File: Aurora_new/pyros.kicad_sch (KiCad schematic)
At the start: 19 parts, among them J10 Screw_Terminal_01x02, J11 Screw_Terminal_01x02, J12 Screw_Terminal_01x04, J13 Screw_Terminal_01x02, J14 Screw_Terminal_01x02, J15 Screw_Terminal_01x02, J2 Screw_Terminal_01x04, J22 Screw_Terminal_01x08, J23 Screw_Terminal_01x08, J24 Screw_Terminal_01x08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

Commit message: regulators mount up
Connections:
- net 3.3V renamed 3V3
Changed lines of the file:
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@@
+		)
+	)
+	(global_label "3V3"
+		(shape input)
+		(at 172.72 73.66 180)
+		(fields_autoplaced yes)
+		(effects
+			(font
+				(size 1.27 1.27)
+			)
+			(justify right)
+		)
+		(property "Intersheetrefs" "${INTERSHEET_REFS}"
+			(at 166.2272 73.66 0)
+			(effects
+				(font
+					(size 1.27 1.27)
+				)
+				(justify right)
+				(hide yes)
+			)
 		)
 	)
@@
 		(property "Intersheetrefs" "${INTERSHEET_REFS}"
 			(at 225.1915 83.82 0)
+			(effects
+				(font
+					(size 1.27 1.27)
+				)
+				(justify right)
+				(hide yes)
+			)
+		)
+	)
+	(global_label "5V"
+		(shape input)
+		(at 168.91 76.2 180)
+		(fields_autoplaced yes)
+		(effects
+			(font
+				(size 1.27 1.27)
+			)
+			(justify right)
+		)
+		(property "Intersheetrefs" "${INTERSHEET_REFS}"
+			(at 163.6267 76.2 0)
 			(effects
 				(font
@@
 		(property "Intersheetrefs" "${INTERSHEET_REFS}"
 			(at 228.4572 55.88 0)
+			(effects
+				(font
+					(size 1.27 1.27)
+				)
+				(justify right)
+				(hide yes)
+			)
+		)
+	)
+	(global_label "5V"
+		(shape input)
+		(at 158.75 129.54 180)
+		(fields_autoplaced yes)
+		(effects
+			(font
+				(size 1.27 1.27)
+			)
+			(justify right)
+		)
+		(property "Intersheetrefs" "${INTERSHEET_REFS}"
+			(at 153.4667 129.54 0)
 			(effects
 				(font
@@
 	)
 	(symbol
-		(lib_id "power:+3.3V")
-		(at 172.72 73.66 0)
-		(unit 1)
-		(exclude_from_sim no)
-		(in_bom yes)
-		(on_board yes)
-		(dnp no)
-		(fields_autoplaced yes)
-		(property "Reference" "#PWR034"
-			(at 172.72 77.47 0)
-			(effects
-				(font
-					(size 1.27 1.27)
-				)
-				(hide yes)
-			)
-		)
-		(property "Value" "3.3V"
-			(at 172.72 68.58 0)
-			(effects
-				(font
-					(size 1.27 1.27)
-				)
-			)
-		)
-		(property "Footprint" ""
-			(at 172.72 73.66 0)
-			(effects
-				(font
-					(size 1.27 1.27)
-				)
-				(hide yes)
-			)
-		)
-		(property "Datasheet" ""
-			(at 172.72 73.66 0)
-			(effects
-				(font
-					(size 1.27 1.27)
-				)
-				(hide yes)
-			)
-		)
-		(property "Description" "Power symbol creates a global label with name \"+3.3V\""
-			(at 172.72 73.66 0)
-			(effects
-				(font
-					(size 1.27 1.27)
-				)
-				(hide yes)
-			)
-		)
-		(pin "1"
-		)
-		(instances
-			(project "Aurora"
-				(path "/073f53a3-faa8-4419-bff2-f325850469a4/b243e184-8694-4e24-9f49-14da58e669df"
-					(reference "#PWR034")
-					(unit 1)
-				)
-			)
-		)
-	)
-	(symbol
 		(lib_id "power:GND")
 		(at 172.72 97.79 0)
@@
 				(path "/073f53a3-faa8-4419-bff2-f325850469a4/b243e184-8694-4e24-9f49-14da58e669df"
 					(reference "J23")
-					(unit 1)
-				)
-			)
-		)
-	)
-	(symbol
-		(lib_id "power:+3.3V")
-		(at 158.75 129.54 0)
-		(unit 1)
-		(exclude_from_sim no)
-		(in_bom yes)
-		(on_board yes)
-		(dnp no)
-		(fields_autoplaced yes)
-		(property "Reference" "#PWR050"
-			(at 158.75 133.35 0)
-			(effects
-				(font
-					(size 1.27 1.27)
-				)
-				(hide yes)
-			)
-		)
-		(property "Value" "5V"
-			(at 158.75 124.46 0)
-			(effects
-				(font
-					(size 1.27 1.27)
-				)
-			)
-		)
-		(property "Footprint" ""
-			(at 158.75 129.54 0)
-			(effects
-				(font
-					(size 1.27 1.27)
-				)
-				(hide yes)
-			)
-		)
-		(property "Datasheet" ""
-			(at 158.75 129.54 0)
-			(effects
-				(font
-					(size 1.27 1.27)
-				)
-				(hide yes)
-			)
-		)
-		(property "Description" "Power symbol creates a global label with name \"+3.3V\""
-			(at 158.75 129.54 0)
-			(effects
-				(font
-					(size 1.27 1.27)
-				)
-				(hide yes)
-			)
-		)
-		(pin "1"
-		)
-		(instances
-			(project "Aurora"
-				(path "/073f53a3-faa8-4419-bff2-f325850469a4/b243e184-8694-4e24-9f49-14da58e669df"
-					(reference "#PWR050")
 					(unit 1)
 				)
@@
 					(unit 1)
 				)
-			)
-		)
-	)
-	(symbol
-		(lib_id "power:+3.3V")
-		(at 168.91 76.2 0)
-		(unit 1)
-		(exclude_from_sim no)
-		(in_bom yes)
-		(on_board yes)
-		(dnp no)
-		(fields_autoplaced yes)
-		(property "Reference" "#PWR033"
-			(at 168.91 80.01 0)
-			(effects
-				(font
-					(size 1.27 1.27)
-				)
-				(hide yes)
-			)
-		)
-		(property "Value" "5V"
-			(at 168.91 71.12 0)
-			(effects
-				(font
-					(size 1.27 1.27)
-				)
-			)
-		)
-		(property "Footprint" ""
-			(at 168.91 76.2 0)
-			(effects
-				(font
-					(size 1.27 1.27)
-				)
-				(hide yes)
-			)
-		)
-		(property "Datasheet" ""
-			(at 168.91 76.2 0)
-			(effects
-				(font
-					(size 1.27 1.27)
-				)
-				(hide yes)
-			)
-		)
-		(property "Description" "Power symbol creates a global label with name \"+3.3V\""
-			(at 168.91 76.2 0)
-			(effects
-				(font
-					(size 1.27 1.27)
-				)
-				(hide yes)
-			)
-		)
-		(pin "1"
-		)
-		(instances
-			(project "Aurora"
-				(path "/073f53a3-faa8-4419-bff2-f325850469a4/b243e184-8694-4e24-9f49-14da58e669df"
-					(reference "#PWR033")
-					(unit 1)
-				)

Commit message: bom updates (purchase links, prices, etc) and switching imu because out of stock
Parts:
- J10, J11, J13, J14, J15, J8: PURCHASE-URL (none) -> https://www.digikey.com/en/products/detail/phoenix-contact/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; Price (none) -> $1.33000
- J12, J2, J33, J34, J35, J7, J9: PURCHASE-URL (none) -> https://www.digikey.com/en/products/detail/phoenix-contact/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; Price (none) -> $2.06500
- J22, J23, J24, J25, J4, J5: PURCHASE-URL (none) -> https://www.digikey.com/en/products/detail/phoenix-contact/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; Price (none) -> $4.07700

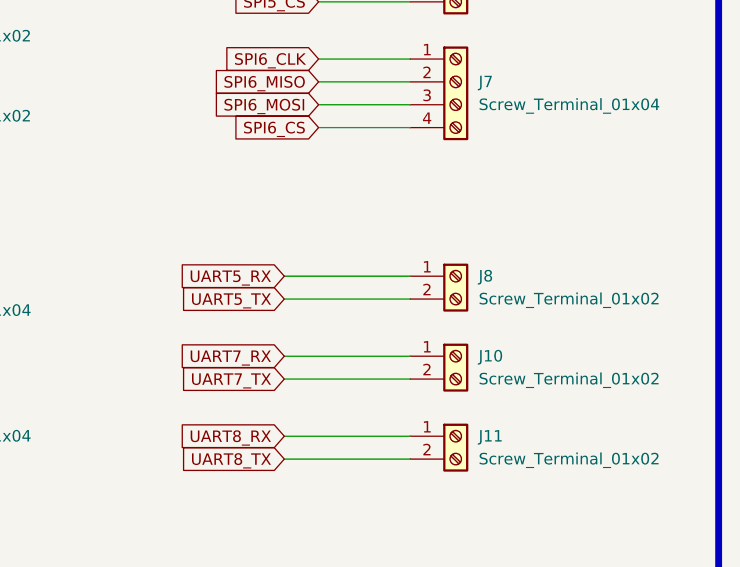
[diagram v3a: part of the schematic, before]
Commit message: working though GPIOs/CSs, Xref with cubeMX
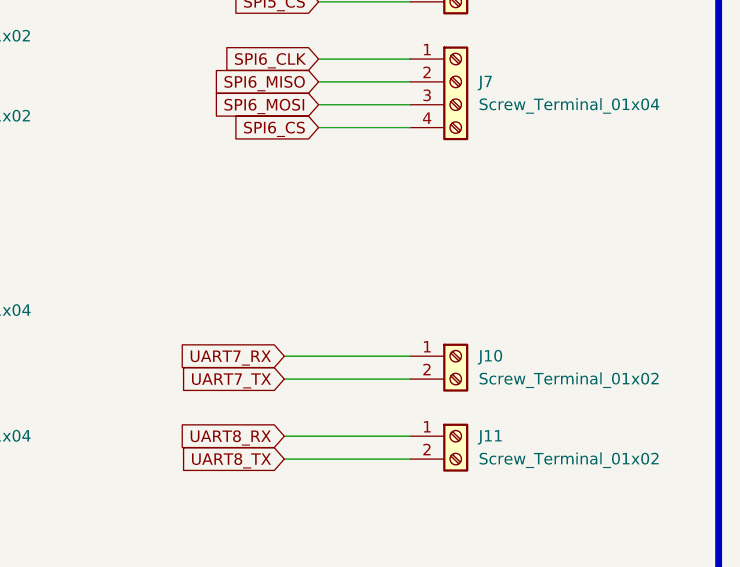
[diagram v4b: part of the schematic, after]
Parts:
- removed J8: Screw_Terminal_01x02, footprints5:CONN_1729128_PXC, symbol Connector:Screw_Terminal_01x02
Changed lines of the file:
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@@
-	(wire
-		(pts
-			(xy 251.46 77.47) (xy 237.49 77.47)
-		)
-		(stroke
-			(width 0)
-			(type default)
-		)
-	)
 	(wire
 		(pts
@@
 		(pts
 			(xy 158.75 129.54) (xy 165.1 129.54)
-		)
-		(stroke
-			(width 0)
-			(type default)
-		)
-	)
-	(wire
-		(pts
-			(xy 251.46 74.93) (xy 237.49 74.93)
 		)
 		(stroke
@@
 		)
 	)
-	(global_label "UART5_RX"
-		(shape input)
-		(at 237.49 74.93 180)
-		(fields_autoplaced yes)
-		(effects
-			(font
-				(size 1.27 1.27)
-			)
-			(justify right)
-		)
-		(property "Intersheetrefs" "${INTERSHEET_REFS}"
-			(at 225.1915 74.93 0)
-			(effects
-				(font
-					(size 1.27 1.27)
-				)
-				(justify right)
-				(hide yes)
-			)
-		)
-	)
 	(global_label "I2C4_SCL"
 		(shape input)
@@
 		(property "Intersheetrefs" "${INTERSHEET_REFS}"
 			(at 22.1124 60.96 0)
-			(effects
-				(font
-					(size 1.27 1.27)
-				)
-				(justify right)
-				(hide yes)
-			)
-		)
-	)
-	(global_label "UART5_TX"
-		(shape input)
-		(at 237.49 77.47 180)
-		(fields_autoplaced yes)
-		(effects
-			(font
-				(size 1.27 1.27)
-			)
-			(justify right)
-		)
-		(property "Intersheetrefs" "${INTERSHEET_REFS}"
-			(at 225.4939 77.47 0)
 			(effects
 				(font
@@
 					(unit 1)
 				)
-			)
-		)
-	)
-	(symbol
-		(lib_id "Connector:Screw_Terminal_01x02")
-		(at 256.54 74.93 0)
-		(unit 1)
-		(exclude_from_sim no)
-		(in_bom yes)
-		(on_board yes)
-		(dnp no)
-		(fields_autoplaced yes)
-		(property "Reference" "J8"
-			(at 259.08 74.9299 0)
-			(effects
-				(font
-					(size 1.27 1.27)
-				)
-				(justify left)
-			)
-		)
-		(property "Value" "Screw_Terminal_01x02"
-			(at 259.08 77.4699 0)
-			(effects
-				(font
-					(size 1.27 1.27)
-				)
-				(justify left)
-			)
-		)
-		(property "Footprint" "footprints5:CONN_1729128_PXC"
-			(at 256.54 74.93 0)
-			(effects
-				(font
-					(size 1.27 1.27)
-				)
-				(hide yes)
-			)
-		)
-		(property "Datasheet" "~"
-			(at 256.54 74.93 0)
-			(effects
-				(font
-					(size 1.27 1.27)
-				)
-				(hide yes)
-			)
-		)
-		(property "Description" "Generic screw terminal, single row, 01x02, script generated (kicad-library-utils/schlib/autogen/connector/)"
-			(at 256.54 74.93 0)
-			(effects
-				(font
-					(size 1.27 1.27)
-				)
-				(hide yes)
-			)
-		)
-		(property "PURCHASE-URL" "https://www.digikey.com/en/products/detail/phoenix-contact/1729128/260615?msockid=2519f0312b83673a161fe62a2a5a66c9"
-			(at 256.54 74.93 0)
-			(effects
-				(font
-					(size 1.27 1.27)
-				)
-				(hide yes)
-			)
-		)
-		(property "Price" " $1.33000"
-			(at 256.54 74.93 0)
-			(effects
-				(font
-					(size 1.27 1.27)
-				)
-				(hide yes)
-			)
-		)
-		(pin "2"
-		)
-		(pin "1"
-		)
-		(instances
-			(project ""
-				(path "/073f53a3-faa8-4419-bff2-f325850469a4/b243e184-8694-4e24-9f49-14da58e669df"
-					(reference "J8")
-					(unit 1)
-				)

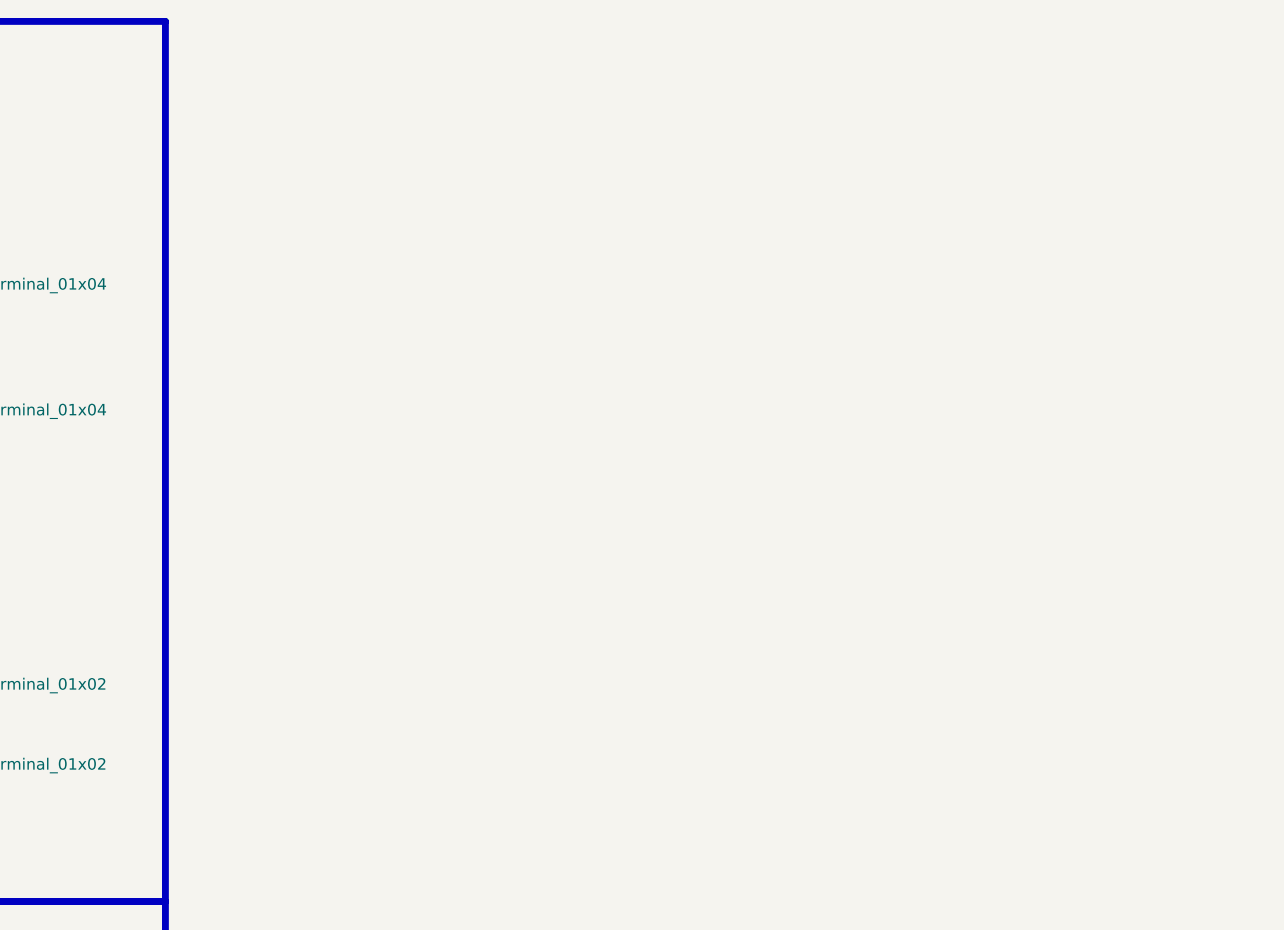
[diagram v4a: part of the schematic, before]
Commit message: done with debug header pins
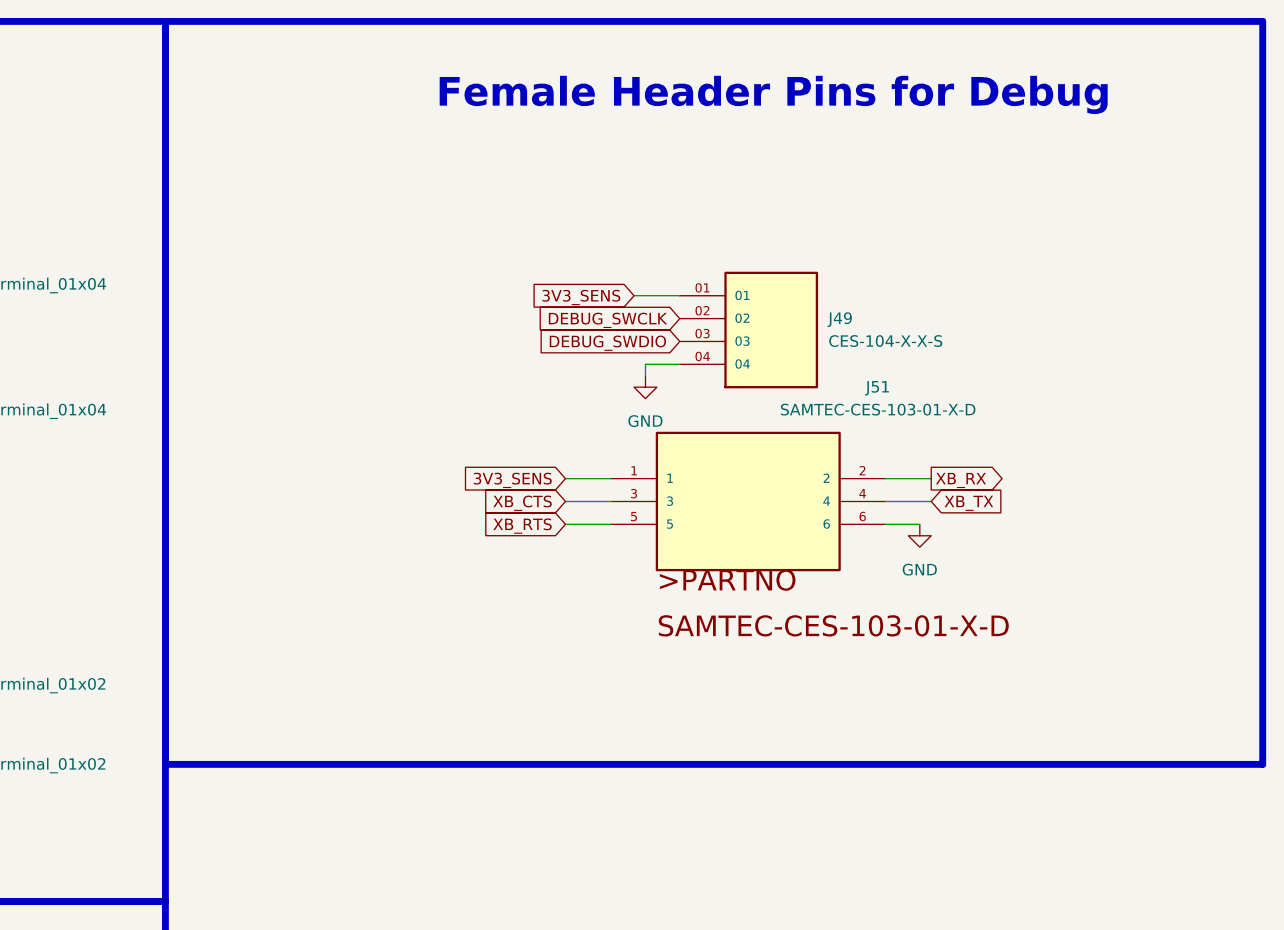
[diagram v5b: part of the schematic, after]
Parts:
- added J49: CES-104-X-X-S, CES_104_01_L_S:SAMTEC_CES-104-X-X-S, symbol CES-104-X-X-S:CES-104-X-X-S
- added J51: SAMTEC-CES-103-01-X-D, CES_103_01_L_D:SAMTEC-CES-103-01-X-D, symbol SAMTEC-CES-103-01-X-D:SAMTEC-CES-103-01-X-D
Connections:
- net GND: now also J49.04, J51.6
- new net 3V3_SENS: J49.01, J51.1
- new net DEBUG_SWCLK: J49.02
- new net DEBUG_SWDIO: J49.03
- new net XB_CTS: J51.3
- new net XB_RTS: J51.5
- new net XB_RX: J51.2
- new net XB_TX: J51.4
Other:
- note added: "Female Header Pins for Debug"

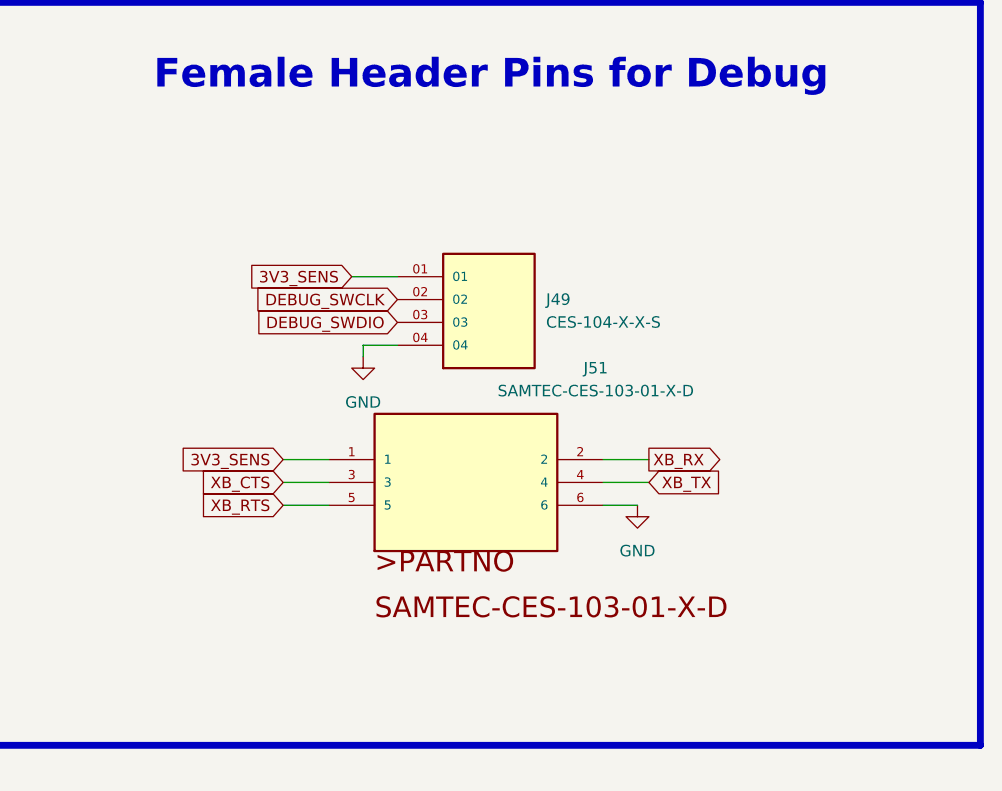
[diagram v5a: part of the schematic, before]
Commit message: fixed header pins, XB on UART
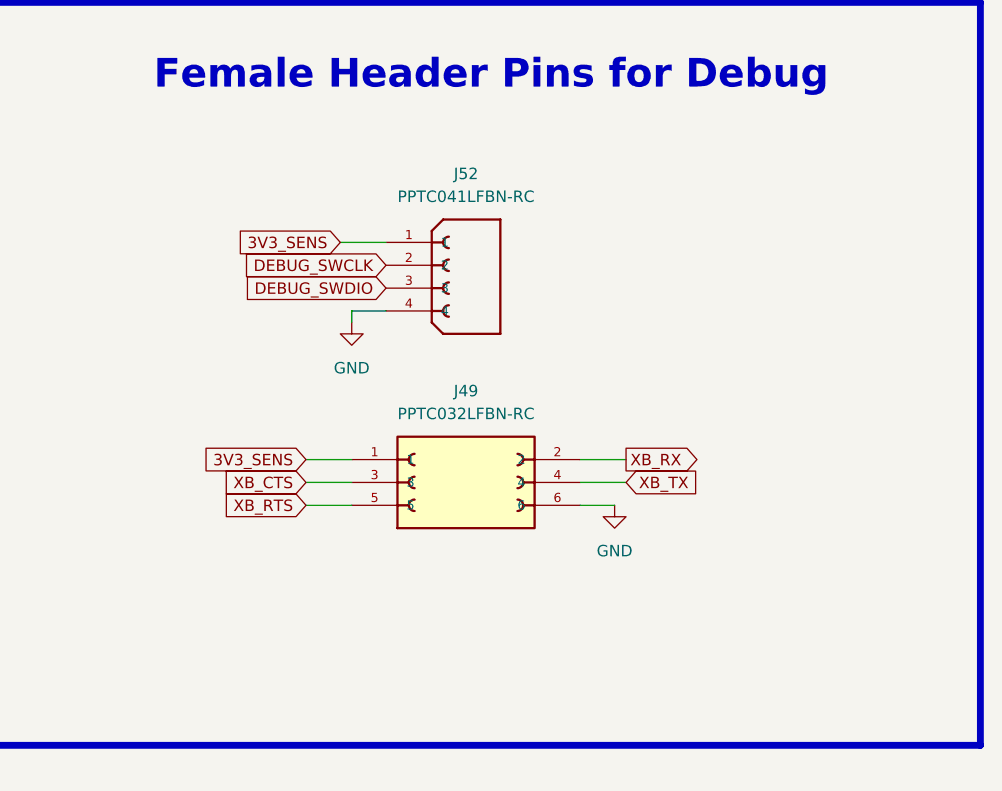
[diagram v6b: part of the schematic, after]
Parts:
- removed J49: CES-104-X-X-S, CES_104_01_L_S:SAMTEC_CES-104-X-X-S, symbol CES-104-X-X-S:CES-104-X-X-S
- removed J51: SAMTEC-CES-103-01-X-D, CES_103_01_L_D:SAMTEC-CES-103-01-X-D, symbol SAMTEC-CES-103-01-X-D:SAMTEC-CES-103-01-X-D
- added J49: PPTC032LFBN-RC, PPTC032LFBN-RC:SULLINS_PPTC032LFBN-RC, symbol PPTC032LFBN-RC:PPTC032LFBN-RC
- added J52: PPTC041LFBN-RC, Connector_PinSocket_2.54mm:PinSocket_1x04_P2.54mm_Vertical, symbol PPTC041LFBN-RC:PPTC041LFBN-RC
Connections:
- net 3V3_SENS: now also J49.1, J52.1
- net DEBUG_SWCLK: now also J52.2
- net DEBUG_SWDIO: now also J52.3
- net GND: now also J49.6, J52.4
- net XB_CTS: now also J49.3
- net XB_RTS: now also J49.5
- net XB_RX: now also J49.2
- net XB_TX: now also J49.4

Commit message: changes to net labelling
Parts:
- J49: footprint PPTC032LFBN-RC:SULLINS_PPTC032LFBN-RC -> Connector_PinSocket_1.00mm:PinSocket_2x03_P1.00mm_Vertical_SMD
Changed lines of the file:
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@@
 			)
 		)
-		(property "Footprint" "PPTC032LFBN-RC:SULLINS_PPTC032LFBN-RC"
+		(property "Footprint" "Connector_PinSocket_1.00mm:PinSocket_2x03_P1.00mm_Vertical_SMD"
 			(at 350.52 66.04 0)
 			(effects
